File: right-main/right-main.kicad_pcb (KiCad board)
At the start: 2 copper layers, 150.4 x 123.8 mm, 209 parts, among them J1 USBCONN, P1 CONN_4, P2 CONN_5, P3 CONN_6, SW1 PTS525SM10, SW11 SPST, SW12 SPST, SW13 SPST, SW14 SPST, SW15 SPST, SW16 SPST, SW17 SPST, SW21 SPST, SW22 SPST, SW23 SPST, SW24 SPST, SW25 SPST, SW26 SPST, SW27 SPST, SW31 SPST, SW32 SPST, SW33 SPST, SW34 SPST, SW35 SPST, SW36 SPST, SW37 SPST, SW41 SPST, SW42 SPST, SW43 SPST, SW44 SPST, SW45 SPST, SW46 SPST, SW47 SPST, SW52 SPST, SW53 SPST, SW54 SPST, SW55 SPST, SW56 SPST, SW57 SPST, U1 ATMEGA32U4, U2 CAT24C256, X1 16Mhz

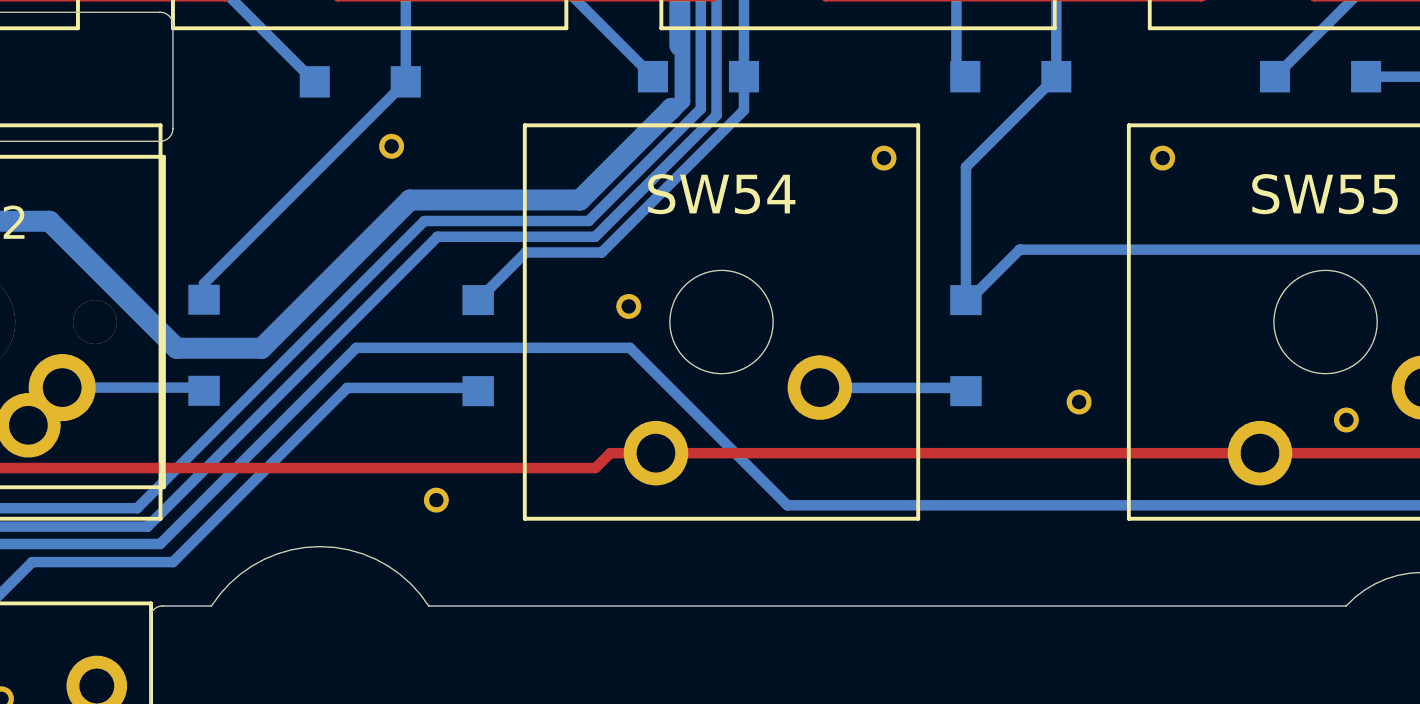
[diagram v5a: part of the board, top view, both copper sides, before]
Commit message: switch 54 right
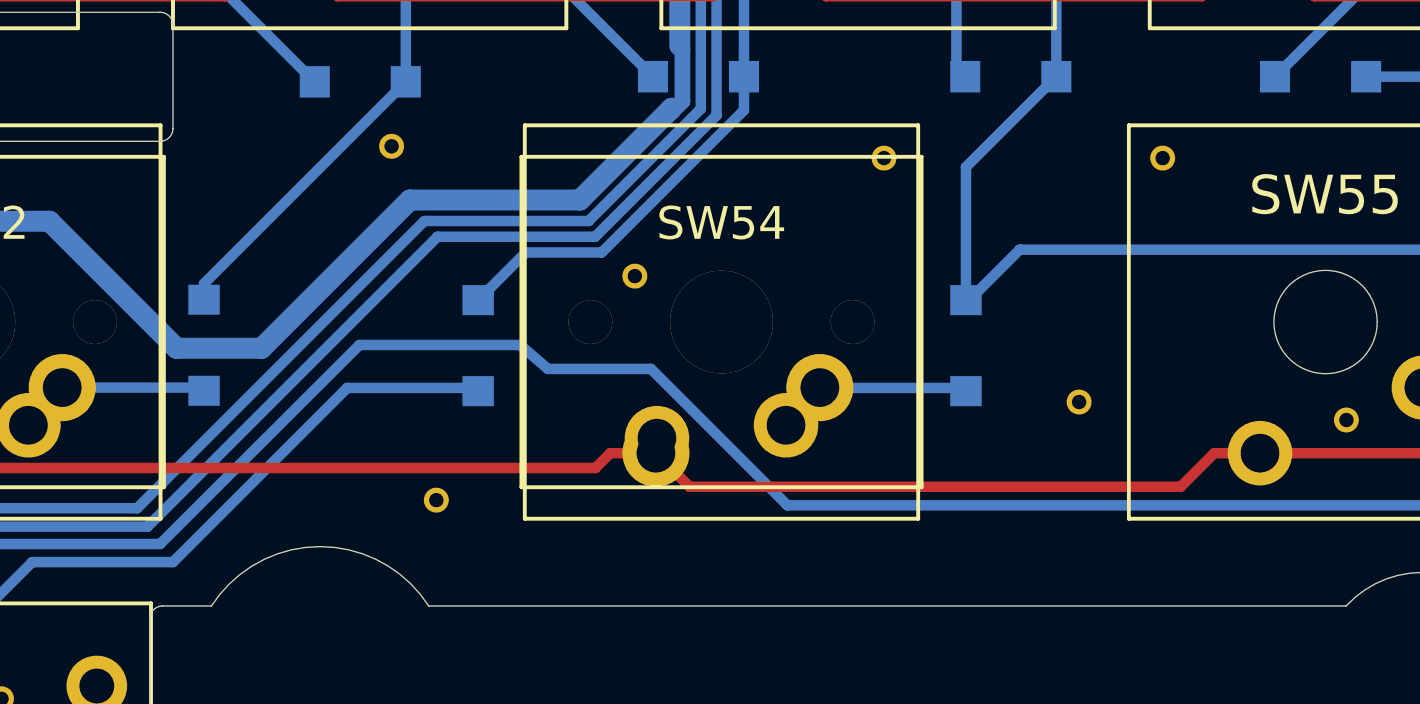
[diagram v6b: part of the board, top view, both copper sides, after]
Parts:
- SW54: footprint UGL:Cherry_MX -> ugl:Cherry-MX-Matias-Hybrid
- moved via 38/22mil 1.20 mm to (159.9, 137.9)
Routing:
- net Net-(D54-Pad2): track 5.67 -> 7.67 mm
- net /ROW5: track 166.2 -> 167.3 mm
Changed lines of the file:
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@@
 (kicad_pcb (version 4) (host pcbnew 4.0.1-stable)
   (general
-    (links 365)
+    (links 367)
     (no_connects 0)
     (area 109.795002 32.293387 260.205001 156.105002)
     (thickness 1.6)
     (drawings 354)
-    (tracks 1128)
+    (tracks 1135)
     (zones 0)
     (modules 209)
@@
   (layers
     (0 F.Cu signal)
-    (31 B.Cu signal hide)
+    (31 B.Cu signal)
     (32 B.Adhes user)
     (33 F.Adhes user)
@@
   )
   (module UGL:via_38_22mil (layer F.Cu)
-    (at 159.657 139.096)
+    (at 159.893 137.922)
     (fp_text reference "via 38/22mil" (at 0 -1.8) (layer F.SilkS) hide
       (effects (font (size 0.75 0.75) (thickness 0.15)))
@@
       (net 20 /ROW5))
   )
-  (module UGL:Cherry_MX locked (layer F.Cu)
-    (at 163.250003 139.7 180)
-    (fp_text reference SW54 (at 0 4.9 180) (layer F.SilkS)
-      (effects (font (size 1.5 1.5) (thickness 0.3)))
-    )
-    (fp_text value SPST (at 0 0 180) (layer F.SilkS) hide
-      (effects (font (size 1.5 1.5) (thickness 0.3)))
-    )
-    (fp_line (start -7.6 -7.6) (end -7.6 7.6) (layer B.SilkS) (width 0.15))
-    (fp_line (start -7.6 7.6) (end 7.6 7.6) (layer B.SilkS) (width 0.15))
-    (fp_line (start 7.6 -7.6) (end 7.6 7.6) (layer B.SilkS) (width 0.15))
-    (fp_line (start -7.6 -7.6) (end 7.6 -7.6) (layer B.SilkS) (width 0.15))
-    (fp_line (start -7.62 -7.62) (end 7.62 -7.62) (layer F.SilkS) (width 0.15))
-    (fp_line (start 7.62 -7.62) (end 7.62 7.62) (layer F.SilkS) (width 0.15))
-    (fp_line (start 7.62 7.62) (end -7.62 7.62) (layer F.SilkS) (width 0.15))
-    (fp_line (start -7.62 7.62) (end -7.62 -7.62) (layer F.SilkS) (width 0.15))
-    (pad "" np_thru_hole circle (at 0 0 180) (size 4 4) (drill 4) (layers *.Cu *.Mask F.SilkS))
-    (pad 2 thru_hole circle (at -3.81 -2.54 180) (size 2.5 2.5) (drill 1.5) (layers *.Cu *.Mask F.SilkS)
-      (net 60 "Net-(D54-Pad2)"))
-    (pad 1 thru_hole circle (at 2.54 -5.08 180) (size 2.5 2.5) (drill 1.5) (layers *.Cu *.Mask F.SilkS)
-      (net 20 /ROW5))
-  )
   (module UGL:UX60-MB-5S8 locked (layer F.Cu)
     (at 175.849803 43.601924 85.4)
@@
     )
   )
+  (module ugl:Cherry-MX-Matias-Hybrid locked (layer F.Cu)
+    (at 163.250003 139.7 180)
+    (tags switch)
+    (fp_text reference SW54 (at 0 3.81 180) (layer F.SilkS)
+      (effects (font (thickness 0.3048)))
+    )
+    (fp_text value SPST (at 0 0 180) (layer F.SilkS) hide
+      (effects (font (thickness 0.3048)))
+    )
+    (fp_line (start -7.62 7.62) (end -7.62 -7.62) (layer B.SilkS) (width 0.15))
+    (fp_line (start 7.62 7.62) (end -7.62 7.62) (layer B.SilkS) (width 0.15))
+    (fp_line (start 7.62 -7.62) (end 7.62 7.62) (layer B.SilkS) (width 0.15))
+    (fp_line (start -7.62 -7.62) (end 7.62 -7.62) (layer B.SilkS) (width 0.15))
+    (fp_line (start -7.75 -6.4) (end -7.75 6.4) (layer F.SilkS) (width 0.15))
+    (fp_line (start 7.75 -6.4) (end 7.75 6.4) (layer F.SilkS) (width 0.15))
+    (fp_line (start -7.75 6.4) (end 7.75 6.4) (layer F.SilkS) (width 0.15))
+    (fp_line (start -7.75 -6.4) (end 7.75 -6.4) (layer F.SilkS) (width 0.15))
+    (fp_line (start -7.62 -7.62) (end 7.62 -7.62) (layer F.SilkS) (width 0.15))
+    (fp_line (start 7.62 -7.62) (end 7.62 7.62) (layer F.SilkS) (width 0.15))
+    (fp_line (start 7.62 7.62) (end -7.62 7.62) (layer F.SilkS) (width 0.15))
+    (fp_line (start -7.62 7.62) (end -7.62 -7.62) (layer F.SilkS) (width 0.15))
+    (pad 0 thru_hole circle (at 0 0 180) (size 3.98018 3.98018) (drill 3.98018) (layers *.Cu *.Mask F.SilkS))
+    (pad 1 thru_hole circle (at 2.54 -5.08 180) (size 2.6 2.6) (drill 1.5011) (layers *.Cu *.Mask F.SilkS)
+      (net 20 /ROW5))
+    (pad 2 thru_hole circle (at -3.81 -2.54 180) (size 2.6 2.6) (drill 1.5011) (layers *.Cu *.Mask F.SilkS)
+      (net 60 "Net-(D54-Pad2)"))
+    (pad "" thru_hole circle (at -5.08 0 180) (size 1.69926 1.69926) (drill 1.69926) (layers *.Cu *.Mask F.SilkS))
+    (pad "" thru_hole circle (at 5.08 0 180) (size 1.69926 1.69926) (drill 1.69926) (layers *.Cu *.Mask F.SilkS))
+    (pad 1 thru_hole circle (at 2.5 -4.5 180) (size 2.5 2.5) (drill 1.5) (layers *.Cu *.Mask F.SilkS)
+      (net 20 /ROW5))
+    (pad 2 thru_hole circle (at -2.5 -4 180) (size 2.5 2.5) (drill 1.5) (layers *.Cu *.Mask F.SilkS)
+      (net 60 "Net-(D54-Pad2)"))
+    (model cherry_mx1.wrl
+      (at (xyz 0 0 0))
+      (scale (xyz 1 1 1))
+      (rotate (xyz 0 0 0))
+    )
+  )
   (gr_line (start 120.857 138.196) (end 121.657 137.396) (angle 90) (layer B.SilkS) (width 0.2))
   (gr_line (start 124.457 148.096) (end 124.457 148.296) (angle 90) (layer B.SilkS) (width 0.2))
@@
   (segment (start 241.06 124.899) (end 241.06 123.24) (width 0.4064) (layer B.Cu) (net 19))
   (segment (start 246.257 130.096) (end 241.06 124.899) (width 0.4064) (layer B.Cu) (net 19))
+  (segment (start 184.109997 144.78) (end 182.342231 144.78) (width 0.4064) (layer F.Cu) (net 20))
+  (segment (start 182.342231 144.78) (end 181.042232 146.079999) (width 0.4064) (layer F.Cu) (net 20))
+  (segment (start 181.042232 146.079999) (end 162.010002 146.079999) (width 0.4064) (layer F.Cu) (net 20))
+  (segment (start 162.010002 146.079999) (end 160.710003 144.78) (width 0.4064) (layer F.Cu) (net 20))
   (segment (start 160.710003 144.78) (end 158.942237 144.78) (width 0.4064) (layer F.Cu) (net 20))
   (segment (start 158.942237 144.78) (end 158.365836 145.356401) (width 0.4064) (layer F.Cu) (net 20))
@@
   (segment (start 238.95 147.3) (end 244.01 142.24) (width 0.4064) (layer F.Cu) (net 20))
   (segment (start 207.509998 144.78) (end 184.109997 144.78) (width 0.4064) (layer F.Cu) (net 20))
-  (segment (start 184.109997 144.78) (end 160.710003 144.78) (width 0.4064) (layer F.Cu) (net 20))
   (segment (start 122.950003 153.189994) (end 122.950003 153.8) (width 0.4064) (layer F.Cu) (net 20))
   (segment (start 131.359997 144.78) (end 122.950003 153.189994) (width 0.4064) (layer F.Cu) (net 20))
@@
   (segment (start 148.7503 142.2527) (end 142.003 149) (width 0.4064) (layer B.Cu) (net 59))
   (segment (start 153.8224 142.2527) (end 148.7503 142.2527) (width 0.4064) (layer B.Cu) (net 59))
+  (segment (start 165.750003 143.7) (end 165.750003 143.55) (width 0.4064) (layer B.Cu) (net 60) (status C00000))
+  (segment (start 165.750003 143.55) (end 167.060003 142.24) (width 0.4064) (layer B.Cu) (net 60) (status C00000))
   (segment (start 167.072703 142.2527) (end 167.060003 142.24) (width 0.4064) (layer B.Cu) (net 60))
   (segment (start 172.72 142.2527) (end 167.072703 142.2527) (width 0.4064) (layer B.Cu) (net 60))
@@
   (segment (start 120.603 147) (end 118.449997 147) (width 0.4064) (layer F.Cu) (net 77))
   (segment (start 122.503 147) (end 120.603 147) (width 0.4064) (layer B.Cu) (net 77))
+  (segment (start 165.803 146.8) (end 160.519099 141.516099) (width 0.4064) (layer B.Cu) (net 78))
+  (segment (start 160.519099 141.516099) (end 156.526024 141.516099) (width 0.4064) (layer B.Cu) (net 78))
+  (segment (start 156.526024 141.516099) (end 155.448 140.589) (width 0.4064) (layer B.Cu) (net 78))
+  (segment (start 155.448 140.589) (end 149.225 140.589) (width 0.4064) (layer B.Cu) (net 78))
+  (segment (start 149.225 140.589) (end 141.503 148.3) (width 0.4064) (layer B.Cu) (net 78))
   (segment (start 211.557 133.096) (end 211.557 136.396) (width 0.4064) (layer B.Cu) (net 78))
   (segment (start 211.557 136.396) (end 216.257 141.096) (width 0.4064) (layer B.Cu) (net 78))
@@
   (segment (start 127.4318 149.9108) (end 121.9138 149.9108) (width 0.4064) (layer B.Cu) (net 78))
   (segment (start 121.9138 149.9108) (end 119.503 147.5) (width 0.4064) (layer B.Cu) (net 78))
-  (segment (start 159.703 140.7) (end 149.103 140.7) (width 0.4064) (layer B.Cu) (net 78))
-  (segment (start 149.103 140.7) (end 141.503 148.3) (width 0.4064) (layer B.Cu) (net 78))
   (segment (start 141.503 148.3) (end 129.0426 148.3) (width 0.4064) (layer B.Cu) (net 78))
   (segment (start 213.503 146.8) (end 165.803 146.8) (width 0.4064) (layer B.Cu) (net 78))
-  (segment (start 165.803 146.8) (end 159.703 140.7) (width 0.4064) (layer B.Cu) (net 78))
   (segment (start 217.012 120.7643) (end 215.815358 120.7643) (width 0.4064) (layer B.Cu) (net 78))
   (segment (start 215.815358 120.7643) (end 213.757 122.822658) (width 0.4064) (layer B.Cu) (net 78))

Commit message: switch 55 right
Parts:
- SW55: footprint UGL:Cherry_MX -> ugl:Cherry-MX-Matias-Hybrid
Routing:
- net Net-(D55-Pad2): track 5.63 -> 7.64 mm
- net /ROW5: track 167.3 -> 168.3 mm
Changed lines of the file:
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@@
     (links 367)
     (no_connects 0)
-    (area 109.795002 32.293387 260.205001 156.105002)
+    (area 19.803 18.9051 270.000001 165.000001)
     (thickness 1.6)
     (drawings 354)
-    (tracks 1135)
+    (tracks 1139)
     (zones 0)
     (modules 209)
@@
       (effects (font (size 0.75 0.75) (thickness 0.15)))
     )
-    (pad "" thru_hole circle (at 0 0) (size 0.9652 0.9652) (drill 0.5588) (layers *.Cu *.Mask F.SilkS)
-      (net 27 GND) (solder_mask_margin -1))
   )
   (module UGL:via_38_22mil (layer F.Cu)
@@
       (effects (font (size 0.75 0.75) (thickness 0.15)))
     )
-    (pad "" thru_hole circle (at 0 0) (size 0.9652 0.9652) (drill 0.5588) (layers *.Cu *.Mask F.SilkS)
-      (net 27 GND) (solder_mask_margin -1))
   )
   (module UGL:via_38_22mil (layer F.Cu)
@@
       (net 20 /ROW5))
   )
-  (module UGL:Cherry_MX locked (layer F.Cu)
-    (at 186.649997 139.7 180)
-    (fp_text reference SW55 (at 0 4.9 180) (layer F.SilkS)
-      (effects (font (size 1.5 1.5) (thickness 0.3)))
-    )
-    (fp_text value SPST (at 0 0 180) (layer F.SilkS) hide
-      (effects (font (size 1.5 1.5) (thickness 0.3)))
-    )
-    (fp_line (start -7.6 -7.6) (end -7.6 7.6) (layer B.SilkS) (width 0.15))
-    (fp_line (start -7.6 7.6) (end 7.6 7.6) (layer B.SilkS) (width 0.15))
-    (fp_line (start 7.6 -7.6) (end 7.6 7.6) (layer B.SilkS) (width 0.15))
-    (fp_line (start -7.6 -7.6) (end 7.6 -7.6) (layer B.SilkS) (width 0.15))
-    (fp_line (start -7.62 -7.62) (end 7.62 -7.62) (layer F.SilkS) (width 0.15))
-    (fp_line (start 7.62 -7.62) (end 7.62 7.62) (layer F.SilkS) (width 0.15))
-    (fp_line (start 7.62 7.62) (end -7.62 7.62) (layer F.SilkS) (width 0.15))
-    (fp_line (start -7.62 7.62) (end -7.62 -7.62) (layer F.SilkS) (width 0.15))
-    (pad "" np_thru_hole circle (at 0 0 180) (size 4 4) (drill 4) (layers *.Cu *.Mask F.SilkS))
-    (pad 2 thru_hole circle (at -3.81 -2.54 180) (size 2.5 2.5) (drill 1.5) (layers *.Cu *.Mask F.SilkS)
-      (net 61 "Net-(D55-Pad2)"))
-    (pad 1 thru_hole circle (at 2.54 -5.08 180) (size 2.5 2.5) (drill 1.5) (layers *.Cu *.Mask F.SilkS)
-      (net 20 /ROW5))
-  )
   (module UGL:UX60-MB-5S8 locked (layer F.Cu)
     (at 175.849803 43.601924 85.4)
@@
     )
   )
+  (module ugl:Cherry-MX-Matias-Hybrid locked (layer F.Cu)
+    (at 186.649997 139.7 180)
+    (tags switch)
+    (fp_text reference SW55 (at 0 3.81 180) (layer F.SilkS)
+      (effects (font (thickness 0.3048)))
+    )
+    (fp_text value SPST (at 0 0 180) (layer F.SilkS) hide
+      (effects (font (thickness 0.3048)))
+    )
+    (fp_line (start -7.62 7.62) (end -7.62 -7.62) (layer B.SilkS) (width 0.15))
+    (fp_line (start 7.62 7.62) (end -7.62 7.62) (layer B.SilkS) (width 0.15))
+    (fp_line (start 7.62 -7.62) (end 7.62 7.62) (layer B.SilkS) (width 0.15))
+    (fp_line (start -7.62 -7.62) (end 7.62 -7.62) (layer B.SilkS) (width 0.15))
+    (fp_line (start -7.75 -6.4) (end -7.75 6.4) (layer F.SilkS) (width 0.15))
+    (fp_line (start 7.75 -6.4) (end 7.75 6.4) (layer F.SilkS) (width 0.15))
+    (fp_line (start -7.75 6.4) (end 7.75 6.4) (layer F.SilkS) (width 0.15))
+    (fp_line (start -7.75 -6.4) (end 7.75 -6.4) (layer F.SilkS) (width 0.15))
+    (fp_line (start -7.62 -7.62) (end 7.62 -7.62) (layer F.SilkS) (width 0.15))
+    (fp_line (start 7.62 -7.62) (end 7.62 7.62) (layer F.SilkS) (width 0.15))
+    (fp_line (start 7.62 7.62) (end -7.62 7.62) (layer F.SilkS) (width 0.15))
+    (fp_line (start -7.62 7.62) (end -7.62 -7.62) (layer F.SilkS) (width 0.15))
+    (pad 0 thru_hole circle (at 0 0 180) (size 3.98018 3.98018) (drill 3.98018) (layers *.Cu *.Mask F.SilkS))
+    (pad 1 thru_hole circle (at 2.54 -5.08 180) (size 2.6 2.6) (drill 1.5011) (layers *.Cu *.Mask F.SilkS)
+      (net 20 /ROW5))
+    (pad 2 thru_hole circle (at -3.81 -2.54 180) (size 2.6 2.6) (drill 1.5011) (layers *.Cu *.Mask F.SilkS)
+      (net 61 "Net-(D55-Pad2)"))
+    (pad "" thru_hole circle (at -5.08 0 180) (size 1.69926 1.69926) (drill 1.69926) (layers *.Cu *.Mask F.SilkS))
+    (pad "" thru_hole circle (at 5.08 0 180) (size 1.69926 1.69926) (drill 1.69926) (layers *.Cu *.Mask F.SilkS))
+    (pad 1 thru_hole circle (at 2.5 -4.5 180) (size 2.5 2.5) (drill 1.5) (layers *.Cu *.Mask F.SilkS)
+      (net 20 /ROW5))
+    (pad 2 thru_hole circle (at -2.5 -4 180) (size 2.5 2.5) (drill 1.5) (layers *.Cu *.Mask F.SilkS)
+      (net 61 "Net-(D55-Pad2)"))
+    (model cherry_mx1.wrl
+      (at (xyz 0 0 0))
+      (scale (xyz 1 1 1))
+      (rotate (xyz 0 0 0))
+    )
+  )
   (gr_line (start 120.857 138.196) (end 121.657 137.396) (angle 90) (layer B.SilkS) (width 0.2))
   (gr_line (start 124.457 148.096) (end 124.457 148.296) (angle 90) (layer B.SilkS) (width 0.2))
@@
   (segment (start 241.06 124.899) (end 241.06 123.24) (width 0.4064) (layer B.Cu) (net 19))
   (segment (start 246.257 130.096) (end 241.06 124.899) (width 0.4064) (layer B.Cu) (net 19))
+  (segment (start 207.509998 144.78) (end 206.209999 146.079999) (width 0.4064) (layer F.Cu) (net 20))
+  (segment (start 206.209999 146.079999) (end 185.409996 146.079999) (width 0.4064) (layer F.Cu) (net 20))
+  (segment (start 185.409996 146.079999) (end 184.109997 144.78) (width 0.4064) (layer F.Cu) (net 20))
   (segment (start 184.109997 144.78) (end 182.342231 144.78) (width 0.4064) (layer F.Cu) (net 20))
   (segment (start 182.342231 144.78) (end 181.042232 146.079999) (width 0.4064) (layer F.Cu) (net 20))
@@
   (segment (start 236.503 147.3) (end 238.95 147.3) (width 0.4064) (layer F.Cu) (net 20))
   (segment (start 238.95 147.3) (end 244.01 142.24) (width 0.4064) (layer F.Cu) (net 20))
-  (segment (start 207.509998 144.78) (end 184.109997 144.78) (width 0.4064) (layer F.Cu) (net 20))
   (segment (start 122.950003 153.189994) (end 122.950003 153.8) (width 0.4064) (layer F.Cu) (net 20))
   (segment (start 131.359997 144.78) (end 122.950003 153.189994) (width 0.4064) (layer F.Cu) (net 20))
@@
   (segment (start 148.7503 142.2527) (end 142.003 149) (width 0.4064) (layer B.Cu) (net 59))
   (segment (start 153.8224 142.2527) (end 148.7503 142.2527) (width 0.4064) (layer B.Cu) (net 59))
-  (segment (start 165.750003 143.7) (end 165.750003 143.55) (width 0.4064) (layer B.Cu) (net 60) (status C00000))
-  (segment (start 165.750003 143.55) (end 167.060003 142.24) (width 0.4064) (layer B.Cu) (net 60) (status C00000))
+  (segment (start 165.750003 143.7) (end 165.750003 143.55) (width 0.4064) (layer B.Cu) (net 60))
+  (segment (start 165.750003 143.55) (end 167.060003 142.24) (width 0.4064) (layer B.Cu) (net 60))
   (segment (start 167.072703 142.2527) (end 167.060003 142.24) (width 0.4064) (layer B.Cu) (net 60))
   (segment (start 172.72 142.2527) (end 167.072703 142.2527) (width 0.4064) (layer B.Cu) (net 60))
+  (segment (start 189.149997 143.7) (end 189.149997 143.55) (width 0.4064) (layer B.Cu) (net 61))
+  (segment (start 189.149997 143.55) (end 190.459997 142.24) (width 0.4064) (layer B.Cu) (net 61))
   (segment (start 190.472697 142.2527) (end 190.459997 142.24) (width 0.4064) (layer B.Cu) (net 61))
   (segment (start 196.088 142.2527) (end 190.472697 142.2527) (width 0.4064) (layer B.Cu) (net 61) (status 10))
